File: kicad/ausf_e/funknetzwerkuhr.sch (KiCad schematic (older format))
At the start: 83 parts, among them J2 Conn_01x04_Male, J4 Conn_01x04_Male, Q10 MMBTA42, Q11 MMBTA42, Q12 MMBTA42, Q13 MMBTA42, Q14 MMBTA42, Q15 MMBTA42, Q16 MMBTA42, Q17 MMBTA42, Q18 MMBTA42, Q19 MMBTA42, Q2 MMBTA42, Q20 MMBTA42, Q21 MMBTA42, Q22 MMBTA42, Q3 MMBTA92, Q4 MMBTA42, Q5 MMBTA92, Q6 MMBTA42, Q7 MMBTA92, Q8 MMBTA42, Q9 MMBTA92, U1 74HC595, U2 74HC595, U3 74HC595, U5 NCP1117-33G, U6 ESP-12E

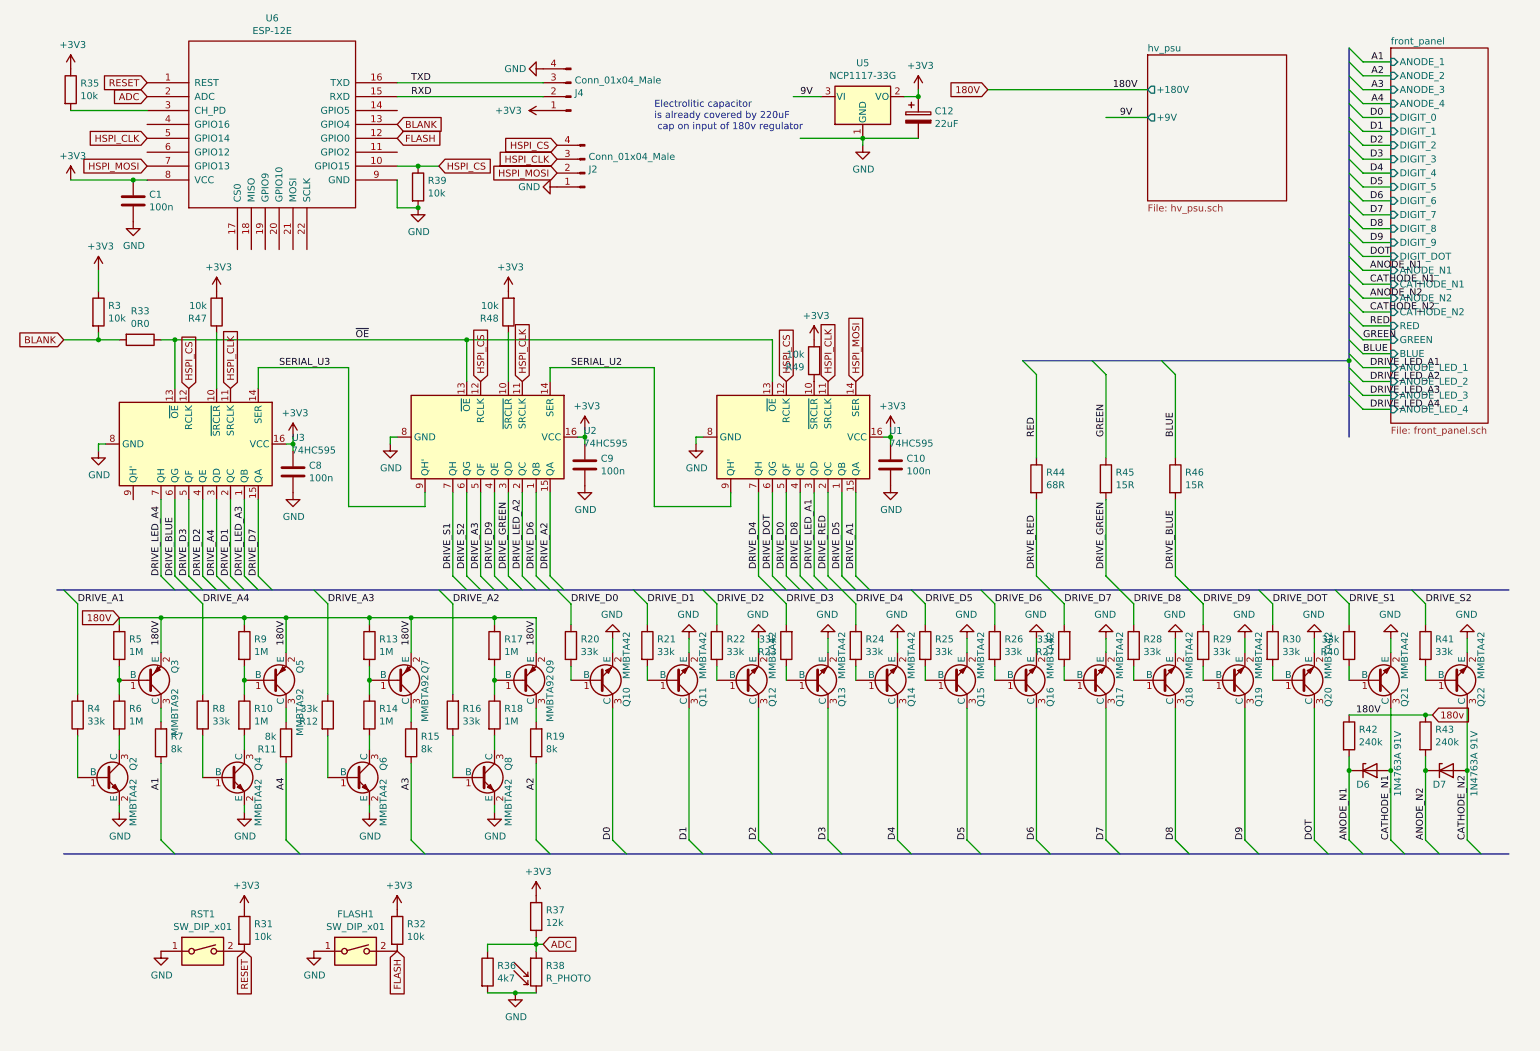
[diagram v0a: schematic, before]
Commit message: Switched from NTPTime to ezTime
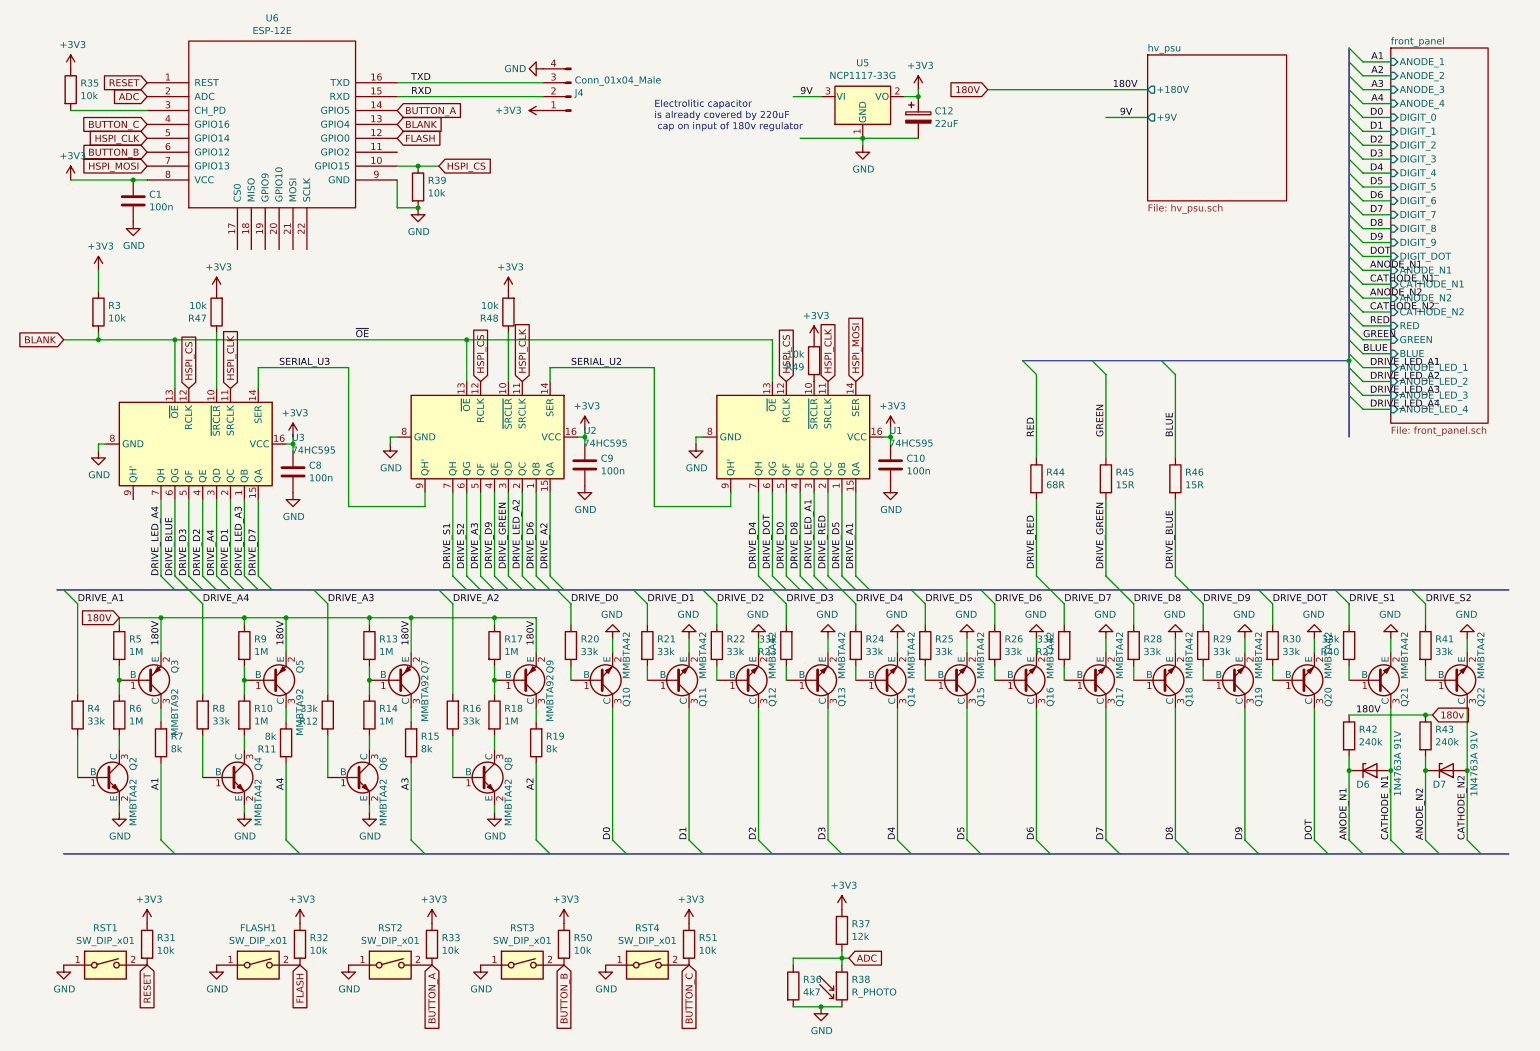
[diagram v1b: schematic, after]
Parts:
- removed J2: Conn_01x04_Male, Connector_PinHeader_2.54mm:PinHeader_1x04_P2.54mm_Vertical, symbol Connector:Conn_01x04_Male
- added R50, R51: 10k, PartsStash:R_0805_2012Metric_Pad1.15x1.40mm_HandSolder_Value, symbol Device:R
- added RST2, RST3, RST4: SW_DIP_x01, Connector_PinHeader_2.54mm:PinHeader_1x02_P2.54mm_Vertical, symbol Switch:SW_DIP_x01
- FLASH1, RST1: footprint Button_Switch_THT:SW_PUSH-12mm -> Connector_PinHeader_2.54mm:PinHeader_1x02_P2.54mm_Vertical
- J4: footprint Connector_PinHeader_2.54mm:PinHeader_1x04_P2.54mm_Horizontal -> Connector_PinHeader_2.54mm:PinHeader_1x04_P2.54mm_Vertical
- R33: value 0R0 -> 10k
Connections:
- net +3V3: now also R33.1, R50.1, R51.1
- net BLANK: now also U1.13 (~OE), U2.13 (~OE), U3.13 (~OE); no longer R33.2
- net GND: now also RST2.1, RST3.1, RST4.1
- net BUTTON_A: now reaches U6.14 (GPIO5)
- net BUTTON_A: now also R33.2, RST2.2
- net BUTTON_C: now reaches U6.4 (GPIO16)
- net BUTTON_C: now also R51.2, RST4.2
- net BUTTON_B: now reaches U6.6 (GPIO12)
- net BUTTON_B: now also R50.2, RST3.2
- removed net ~OE: R33.1, U1.13 (~OE), U2.13 (~OE), U3.13 (~OE)
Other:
- moved on the sheet: FLASH1, R31, R32, R36, R37, R38, RST1
